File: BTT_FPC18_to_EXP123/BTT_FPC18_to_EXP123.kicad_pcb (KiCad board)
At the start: 4 copper layers, 74 x 35 mm, 8 parts, among them J1 FPC18, J2 EXP1, J3 EXP2, J4 EXP3

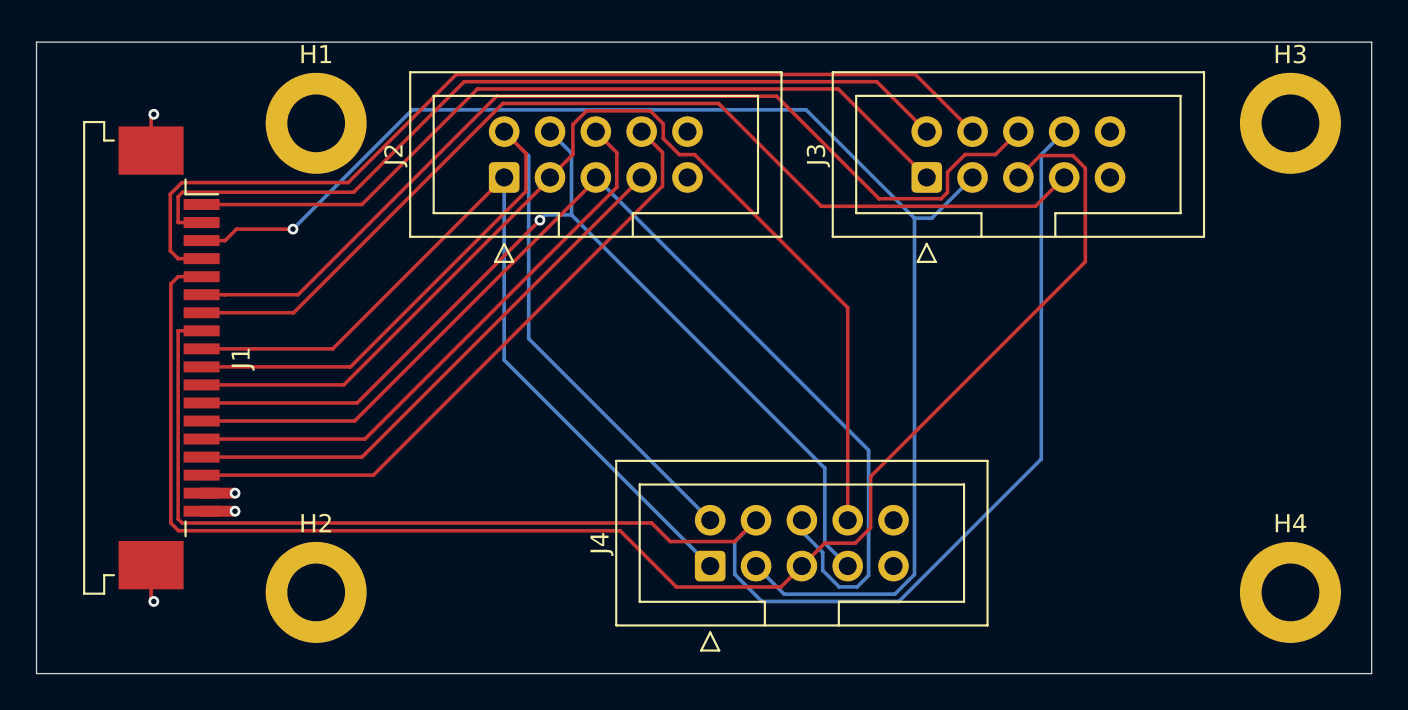
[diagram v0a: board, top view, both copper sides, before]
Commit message: Adjusted some trace routings
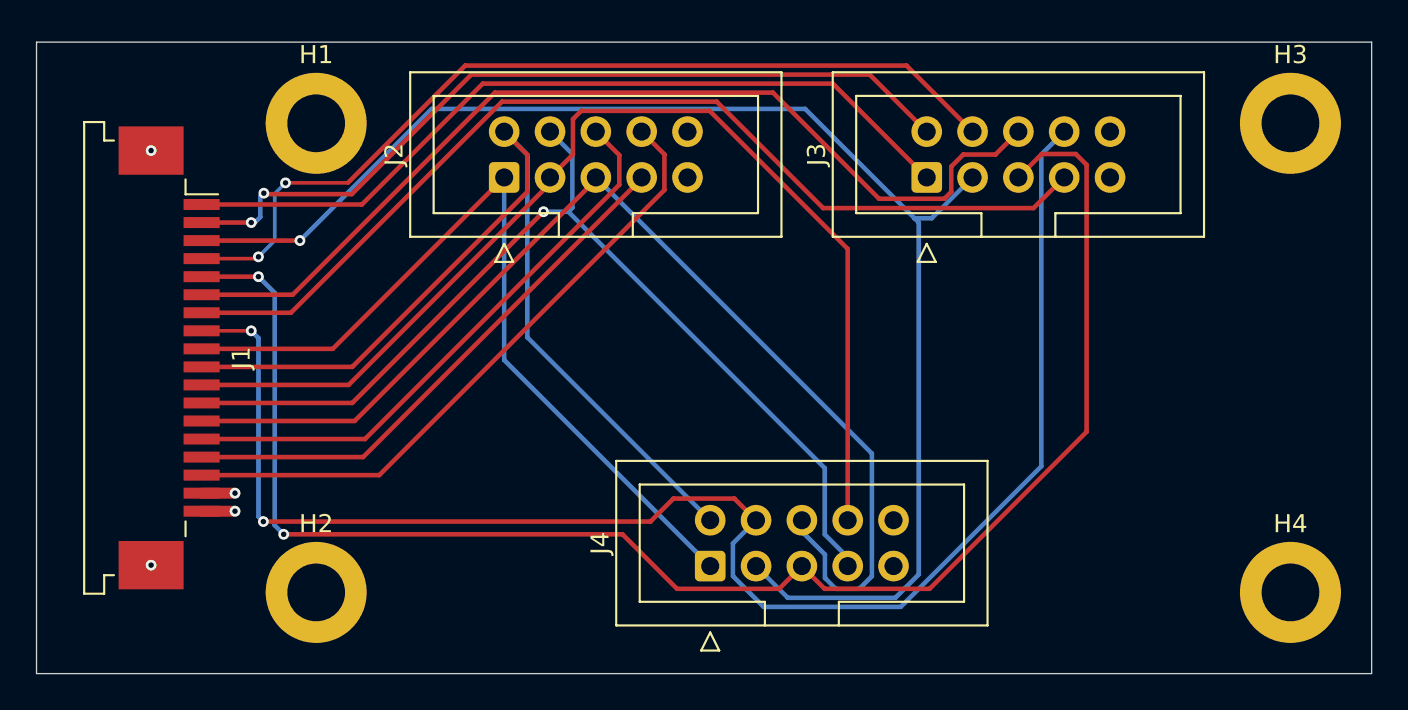
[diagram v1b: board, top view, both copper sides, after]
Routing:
- net GND: track 5.99 -> 1.99 mm
- net /SD_SS: track 53.6 -> 50.2 mm, vias 0 -> 2
- net /SCK: track 48.0 -> 45.6 mm, vias 0 -> 2
- net /RESET: track 87.8 -> 85.7 mm, vias 0 -> 2
- net /BTN_EN2: track 86.1 -> 87.9 mm, vias 0 -> 2
- net /LCD_EN: track 59.9 -> 61.7 mm
- net /LCD_D4: track 62.3 -> 62.8 mm
